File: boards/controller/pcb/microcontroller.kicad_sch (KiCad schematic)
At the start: 4 parts, among them J1 USB_C_Receptacle, U1 STM32U575RITx, U2 TCPP01-M12, U3 ISZ065N03L5SATMA1

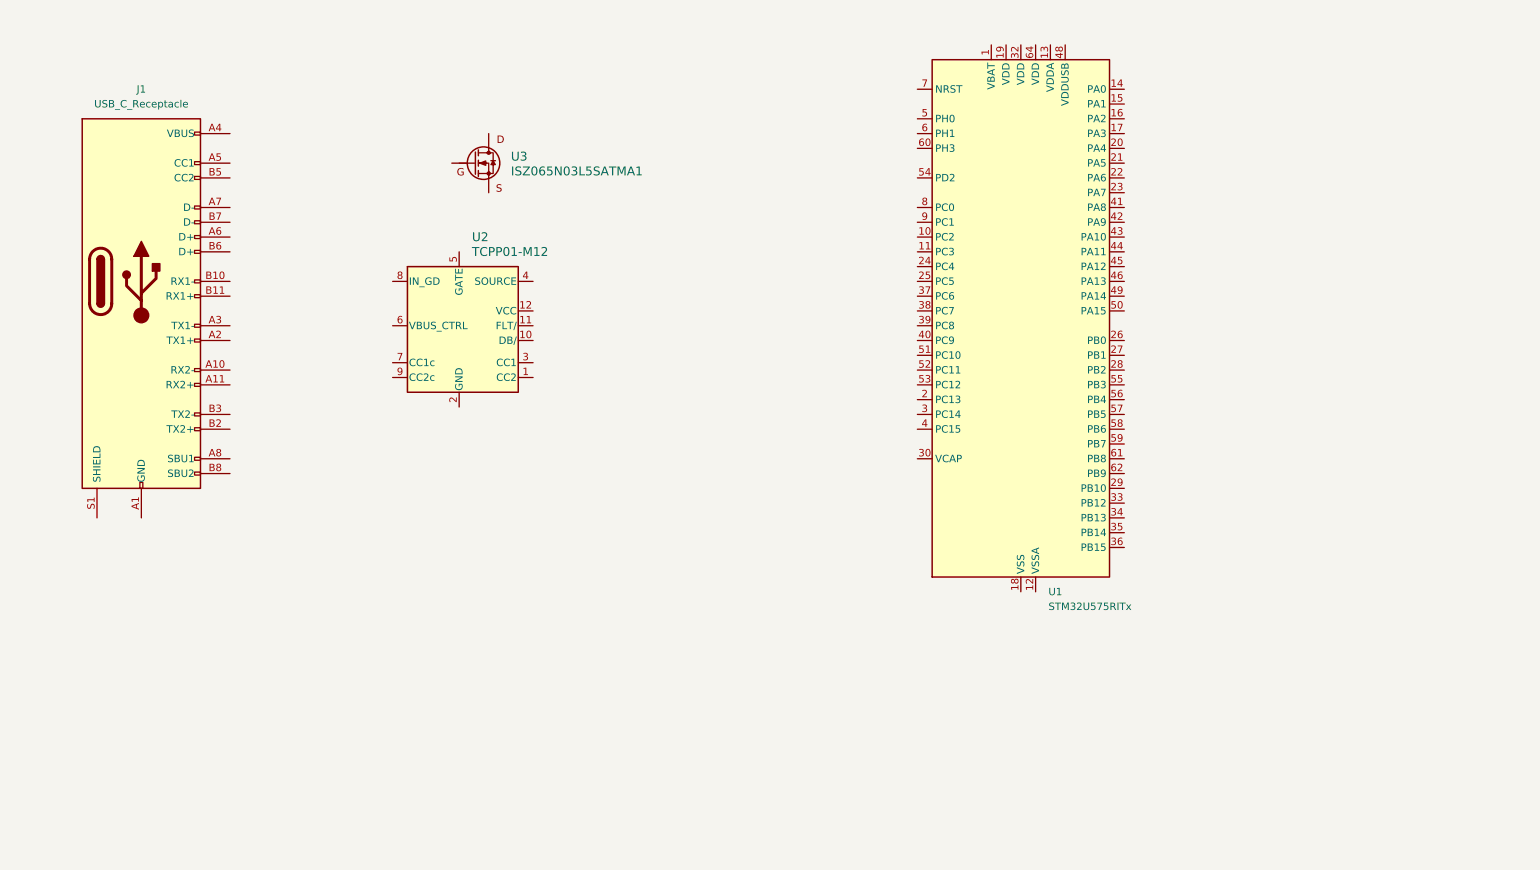
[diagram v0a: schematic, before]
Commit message: controller: Update PCB
Signed-off-by: Nicholas Loehrke <nicholasnloehrke@gmail.com>
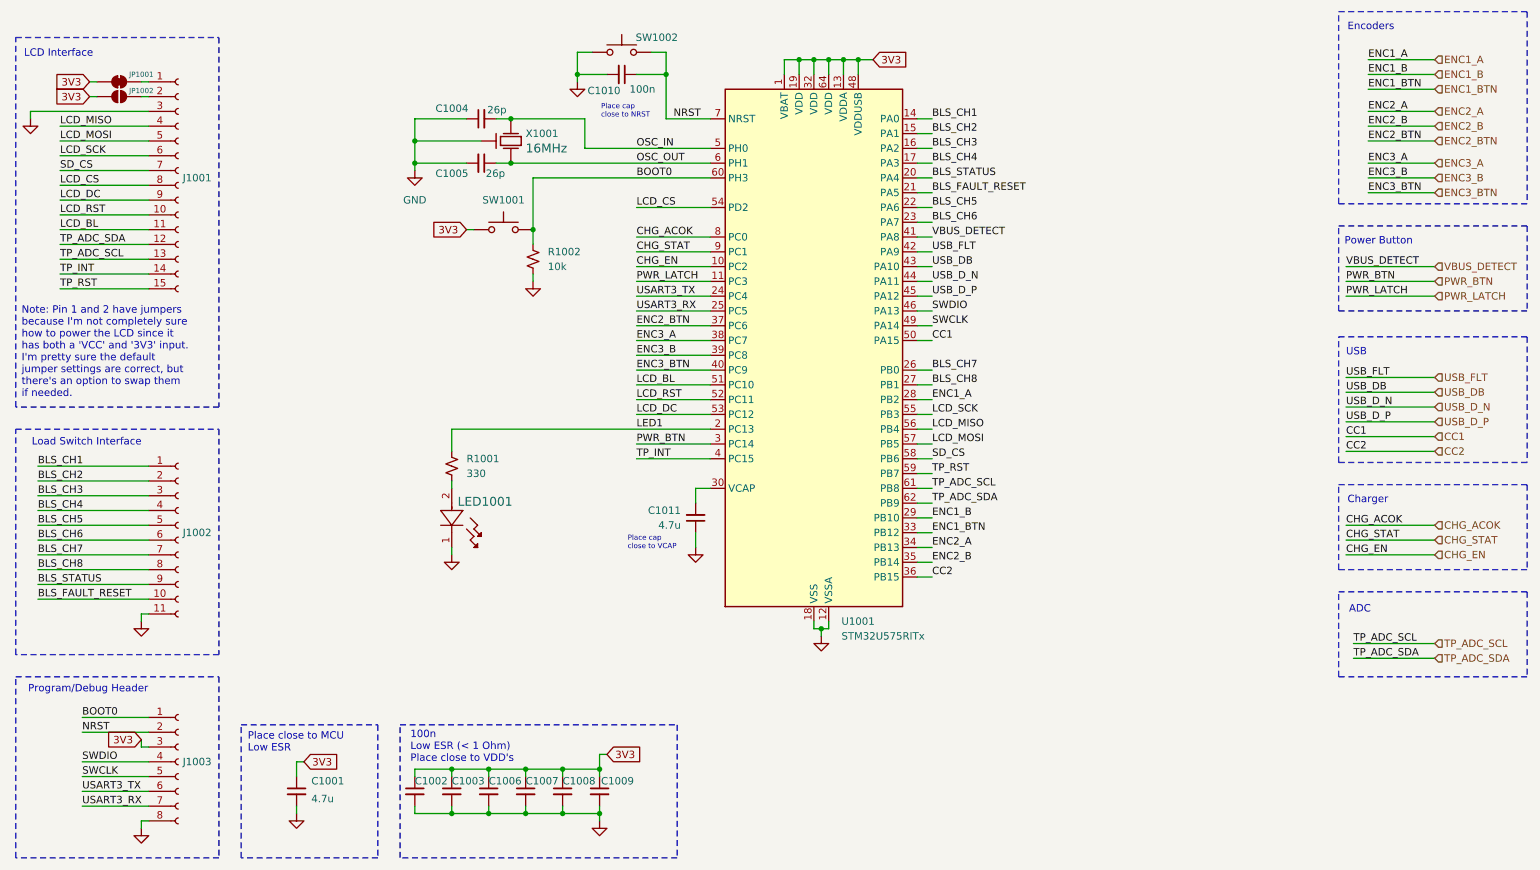
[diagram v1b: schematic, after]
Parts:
- removed J1: USB_C_Receptacle, symbol Connector:USB_C_Receptacle
- removed U1: STM32U575RITx, Package_QFP:LQFP-64_10x10mm_P0.5mm, symbol MCU_ST_STM32U5:STM32U575RITx
- removed U2: TCPP01-M12, QFN12_TCPP01-M12_STM, symbol TCPP01-M12:TCPP01-M12
- removed U3: ISZ065N03L5SATMA1, PG-TSDSON-8-25, symbol ISZ065N03L5SATMA1:ISZ065N03L5SATMA1
- added C1001, C1011: 4.7u, symbol Device:C_Small
- added C1002, C1003, C1006, C1007, C1008, C1009, C1010: 100n, symbol Device:C_Small
- added C1004, C1005: 26p, symbol Device:C_Small
- added J1001: Conn_01x15_Socket, symbol Connector:Conn_01x15_Socket
- added J1002: Conn_01x11_Socket, symbol Connector:Conn_01x11_Socket
- added J1003: Conn_01x08_Socket, symbol Connector:Conn_01x08_Socket
- added JP1001: SolderJumper_2_Bridged, symbol Jumper:SolderJumper_2_Bridged
- added JP1002: SolderJumper_2_Open, symbol Jumper:SolderJumper_2_Open
- added LED1001: B1911PG--20D000514U1930, LED_B1911PG--20D000514U1930_HVK, symbol B1911PG__20D000514U1930:B1911PG--20D000514U1930
- added R1001: 330, symbol Device:R_Small_US
- added R1002: 10k, symbol Device:R_Small_US
- added SW1001, SW1002: SW_Push, symbol Switch:SW_Push
- added U1001: STM32U575RITx, Package_QFP:LQFP-64_10x10mm_P0.5mm, symbol MCU_ST_STM32U5:STM32U575RITx
- added X1001: 16MHz, RH100-16.000-18-2030-EXT-TR_RAL, symbol RH100-16.000-18-2030-EXT-TR:RH100-16.000-18-2030-EXT-TR
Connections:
- new net: LED1001.2, R1001.2
- new net: J1001.1 (Pin_1), JP1001.2 (B)
- new net: J1001.2 (Pin_2), JP1002.2 (B)
- new net: C1011.2, U1001.30 (VCAP)
- new net 3V3: C1001.1, C1002.1, C1003.1, C1006.1, C1007.1, C1008.1, C1009.1, J1003.3 (Pin_3), JP1001.1 (A), JP1002.1 (A), SW1001.1, U1001.1 (VBAT), U1001.13 (VDDA), U1001.19 (VDD), U1001.32 (VDD), U1001.48 (VDDUSB), U1001.64 (VDD)
- new net BLS_CH1: J1002.1 (Pin_1), U1001.14 (PA0)
- new net BLS_CH2: J1002.2 (Pin_2), U1001.15 (PA1)
- new net BLS_CH3: J1002.3 (Pin_3), U1001.16 (PA2)
- new net BLS_CH4: J1002.4 (Pin_4), U1001.17 (PA3)
- new net BLS_CH5: J1002.5 (Pin_5), U1001.22 (PA6)
- new net BLS_CH6: J1002.6 (Pin_6), U1001.23 (PA7)
- new net BLS_CH7: J1002.7 (Pin_7), U1001.26 (PB0)
- new net BLS_CH8: J1002.8 (Pin_8), U1001.27 (PB1)
- new net BLS_FAULT_RESET: J1002.10 (Pin_10), U1001.21 (PA5)
- new net BLS_STATUS: J1002.9 (Pin_9), U1001.20 (PA4)
- new net BOOT0: J1003.1 (Pin_1), R1002.1, SW1001.2, U1001.60 (PH3)
- new net CC1: U1001.50 (PA15)
- new net CC2: U1001.36 (PB15)
- new net CHG_ACOK: U1001.8 (PC0)
- new net CHG_EN: U1001.10 (PC2)
- new net CHG_STAT: U1001.9 (PC1)
- new net ENC1_A: U1001.28 (PB2)
- new net ENC1_B: U1001.29 (PB10)
- new net ENC1_BTN: U1001.33 (PB12)
- new net ENC2_A: U1001.34 (PB13)
- new net ENC2_B: U1001.35 (PB14)
- new net ENC2_BTN: U1001.37 (PC6)
- new net ENC3_A: U1001.38 (PC7)
- new net ENC3_B: U1001.39 (PC8)
- new net ENC3_BTN: U1001.40 (PC9)
- new net GND: C1001.2, C1002.2, C1003.2, C1004.1, C1005.2, C1006.2, C1007.2, C1008.2, C1009.2, C1010.2, C1011.1, J1001.3 (Pin_3), J1002.11 (Pin_11), J1003.8 (Pin_8), LED1001.1, R1002.2, SW1002.1, U1001.12 (VSSA), U1001.18 (VSS), U1001.31 (VSS), U1001.47 (VSS), U1001.63 (VSS), X1001.2, X1001.4
- new net LCD_BL: J1001.11 (Pin_11), U1001.51 (PC10)
- new net LCD_CS: J1001.8 (Pin_8), U1001.54 (PD2)
- new net LCD_DC: J1001.9 (Pin_9), U1001.53 (PC12)
- new net LCD_MISO: J1001.4 (Pin_4), U1001.56 (PB4)
- new net LCD_MOSI: J1001.5 (Pin_5), U1001.57 (PB5)
- new net LCD_RST: J1001.10 (Pin_10), U1001.52 (PC11)
- new net LCD_SCK: J1001.6 (Pin_6), U1001.55 (PB3)
- new net LED1: R1001.1, U1001.2 (PC13)
- new net NRST: C1010.1, J1003.2 (Pin_2), SW1002.2, U1001.7 (NRST)
- new net OSC_IN: C1004.2, U1001.5 (PH0), X1001.1
- new net OSC_OUT: C1005.1, U1001.6 (PH1), X1001.3
- new net PWR_BTN: U1001.3 (PC14)
- new net PWR_LATCH: U1001.11 (PC3)
- new net SD_CS: J1001.7 (Pin_7), U1001.58 (PB6)
- new net SWCLK: J1003.5 (Pin_5), U1001.49 (PA14)
- new net SWDIO: J1003.4 (Pin_4), U1001.46 (PA13)
- new net TP_ADC_SCL: J1001.13 (Pin_13), U1001.61 (PB8)
- new net TP_ADC_SDA: J1001.12 (Pin_12), U1001.62 (PB9)
- new net TP_INT: J1001.14 (Pin_14), U1001.4 (PC15)
- new net TP_RST: J1001.15 (Pin_15), U1001.59 (PB7)
- new net USART3_RX: J1003.7 (Pin_7), U1001.25 (PC5)
- new net USART3_TX: J1003.6 (Pin_6), U1001.24 (PC4)
- new net USB_DB: U1001.43 (PA10)
- new net USB_D_N: U1001.44 (PA11)
- new net USB_D_P: U1001.45 (PA12)
- new net USB_FLT: U1001.42 (PA9)
- new net VBUS_DETECT: U1001.41 (PA8)
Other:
- note added: "100n Low ESR (< 1 Ohm) Place close to VDD's"
- note added: "ADC"
- note added: "Charger"
- note added: "Encoders"
- note added: "LCD Interface"
- note added: "Load Switch Interface"
- note added: "Note: Pin 1 and 2 have jumpers because I'm not completely sure how to power the LCD since it has both a 'VCC' and '3V3' input. I'm pretty sure the default jumper settings are correct, but there's an option to swap them if needed."
- note added: "Place cap close to NRST"
- note added: "Place cap close to VCAP"
- note added: "Place close to MCU Low ESR"
- note added: "Power Button"
- note added: "Program/Debug Header"
- note added: "USB"
